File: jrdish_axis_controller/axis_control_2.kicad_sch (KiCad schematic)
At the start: 36 parts, among them CN12 KF2EDGR-2.54-9P, CN13 KF2EDGR-2.54-6P, Q7 BSS138, Q8 BSS138

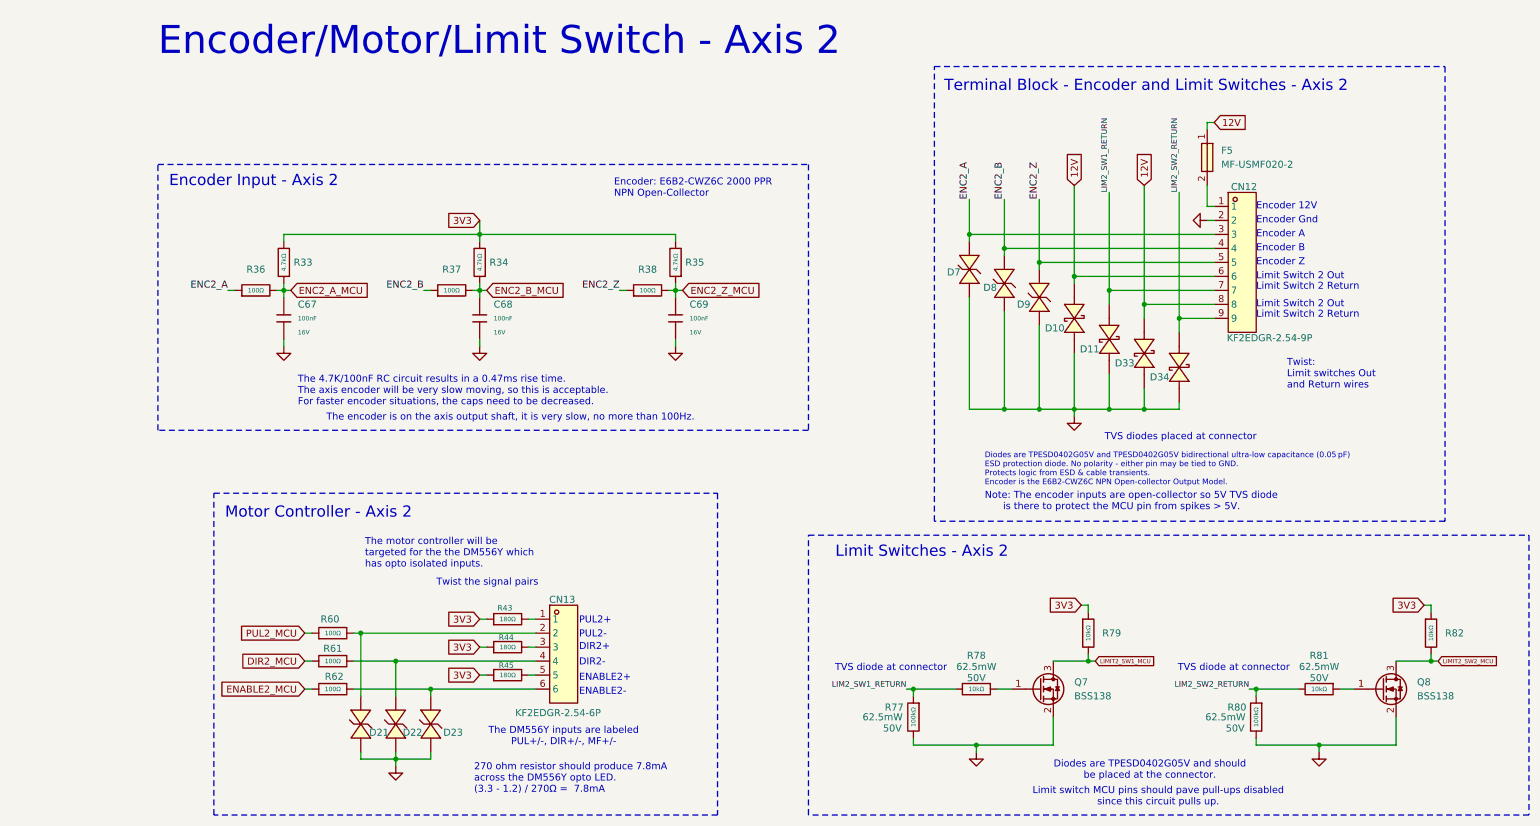
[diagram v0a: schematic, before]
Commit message: Updates for replacing 10k resistors and encoder RC.
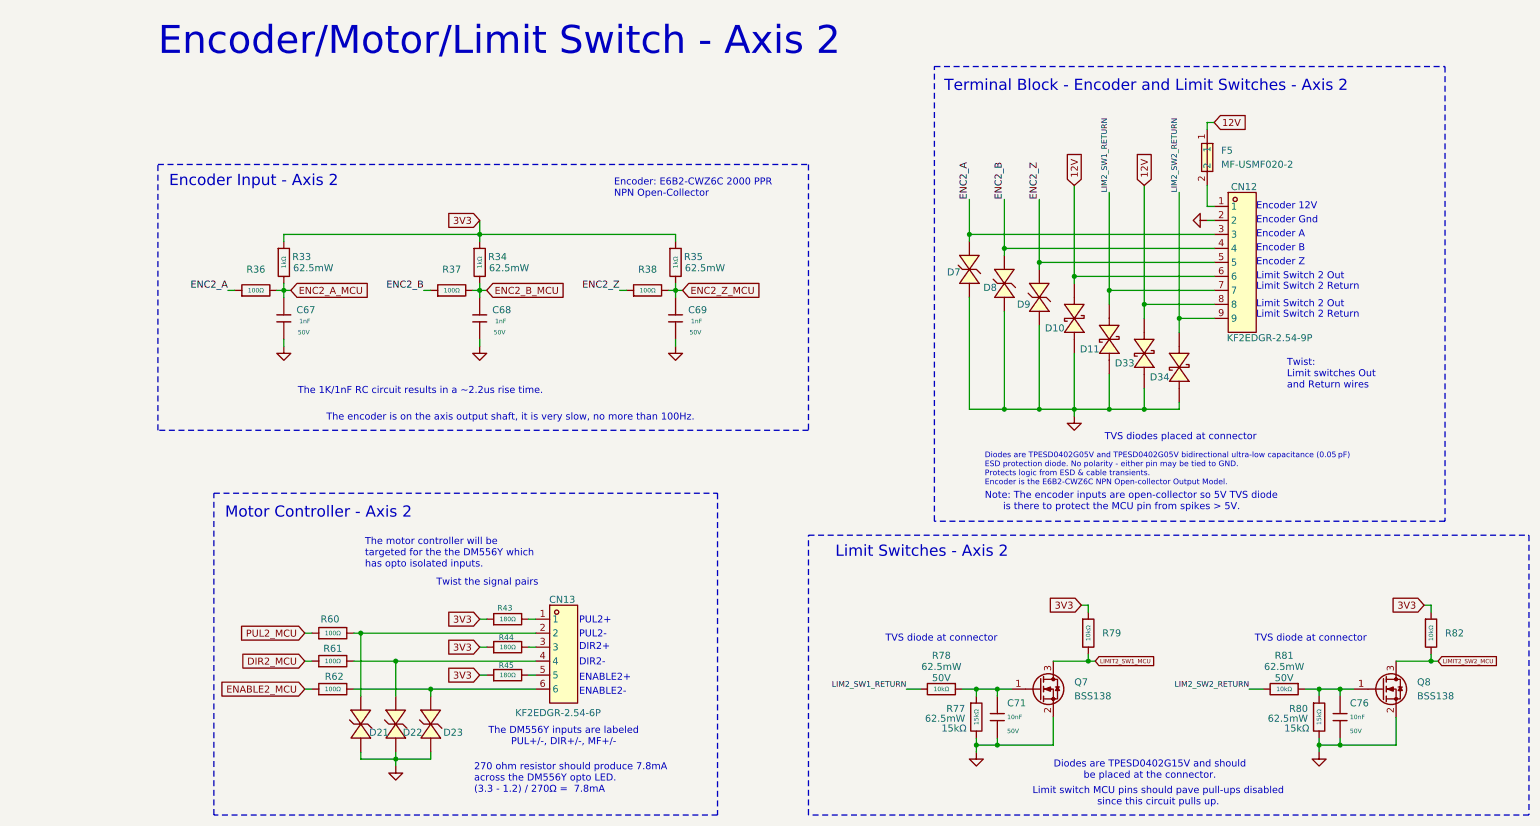
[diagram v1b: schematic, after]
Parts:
- removed C67, C68, C69: 100nF, PCM_JLCPCB:C_0402, symbol PCM_JLCPCB-Capacitors:0402,100nF
- removed R33, R34, R35: 4.7kΩ, PCM_JLCPCB:R_0402, symbol PCM_JLCPCB-Resistors:0402,4.7kΩ
- removed R77, R80: 100kΩ, PCM_JLCPCB:R_0402, symbol PCM_JLCPCB-Resistors:0402,100kΩ
- added C67, C68, C69: 1nF, PCM_JLCPCB:C_0402, symbol PCM_JLCPCB-Capacitors:0402,1nF
- added C71, C76: 10nF, PCM_JLCPCB:C_0603, symbol PCM_JLCPCB-Capacitors:0603,10nF
- added R33, R34, R35: 1kΩ, PCM_JLCPCB:R_0402, symbol PCM_JLCPCB-Resistors:0402,1kΩ
- added R77, R80: 15kΩ, PCM_JLCPCB:R_0402, symbol PCM_JLCPCB-Resistors:0402,15kΩ
- Q7, Q8: KiLib_Generator (none) -> package/gullwing
- R36, R37, R38, R60, R61, R62: Field4 (none) -> ${REFERENCE}
- R78, R79, R81, R82: Field4 (none) -> ${REFERENCE}; LCSC C25744 -> C173683
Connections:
- net 3V3: now also R33.1, R34.1, R35.1
- net ENC2_A_MCU: now also C67.1, R33.2
- net ENC2_B_MCU: now also C68.1, R34.2
- net ENC2_Z_MCU: now also C69.1, R35.2
- net GND: now also C67.2, C68.2, C69.2, C71.2, C76.2, R77.2, R80.2
- net at Q8.1 (G), R81.1: now also C76.1, R80.1
- net at Q7.1 (G), R78.1: now also C71.1, R77.1
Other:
- note added: "Diodes are TPESD0402G15V and should be placed at the connector."
- note added: "The 1K/1nF RC circuit results in a ~2.2us rise time."
- note removed: "Diodes are TPESD0402G05V and should be placed at the connector."
- note removed: "The 4.7K/100nF RC circuit results in a 0.47ms rise time. The axis encoder will be very slow moving, so this is acceptable. For faster encoder situations, the caps need to be decreased."
- moved on the sheet: R78, R81
